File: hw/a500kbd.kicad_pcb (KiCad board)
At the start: 2 copper layers, 49.9 x 51.6 mm, 17 parts, among them J1 SERIAL, J2 AVR-ISP-6, J3 ps2ribbon, J4 ps2ribbon, SW1 SW_DPDT_x2, U1 ATmega88-20P, U2 internal keyboard, U3 ps2conn, U4 mainboard kb conn., Y1 14.7456MHz

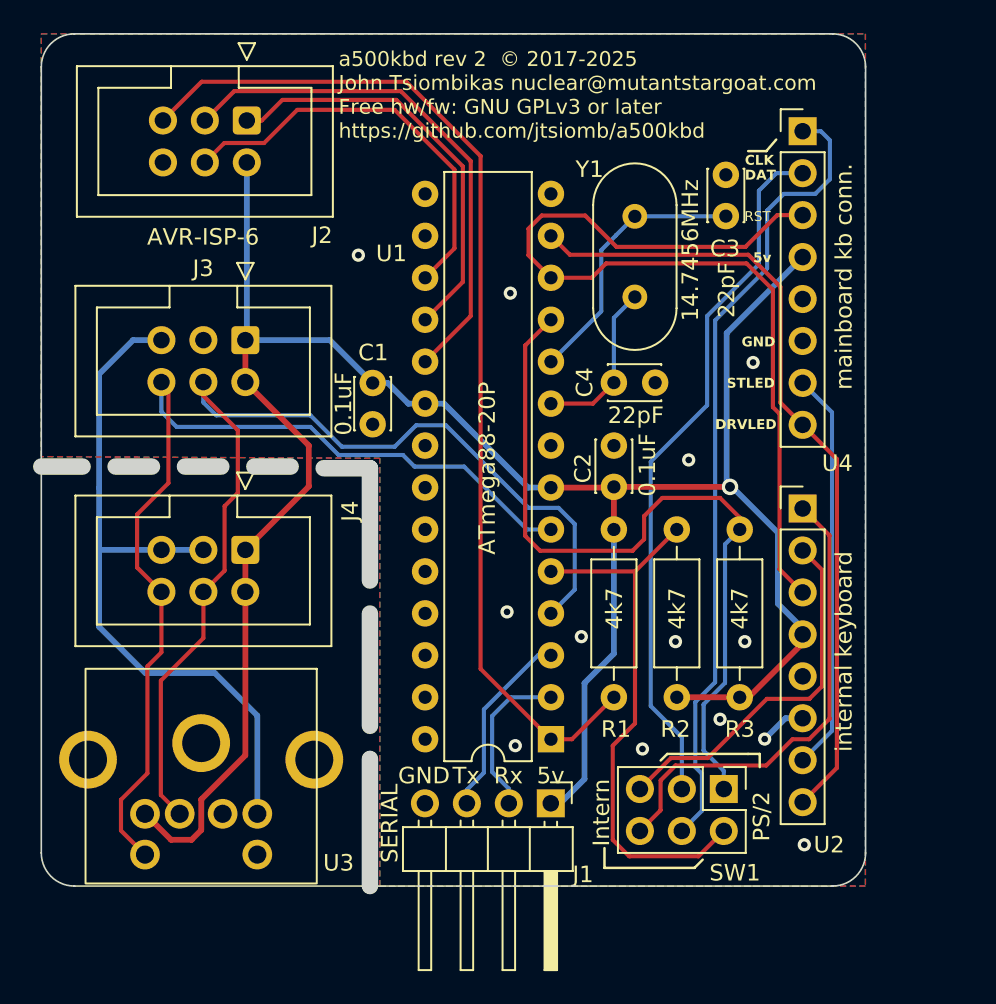
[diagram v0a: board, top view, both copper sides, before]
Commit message: fix pcb cutouts and minor re-routing of a signal
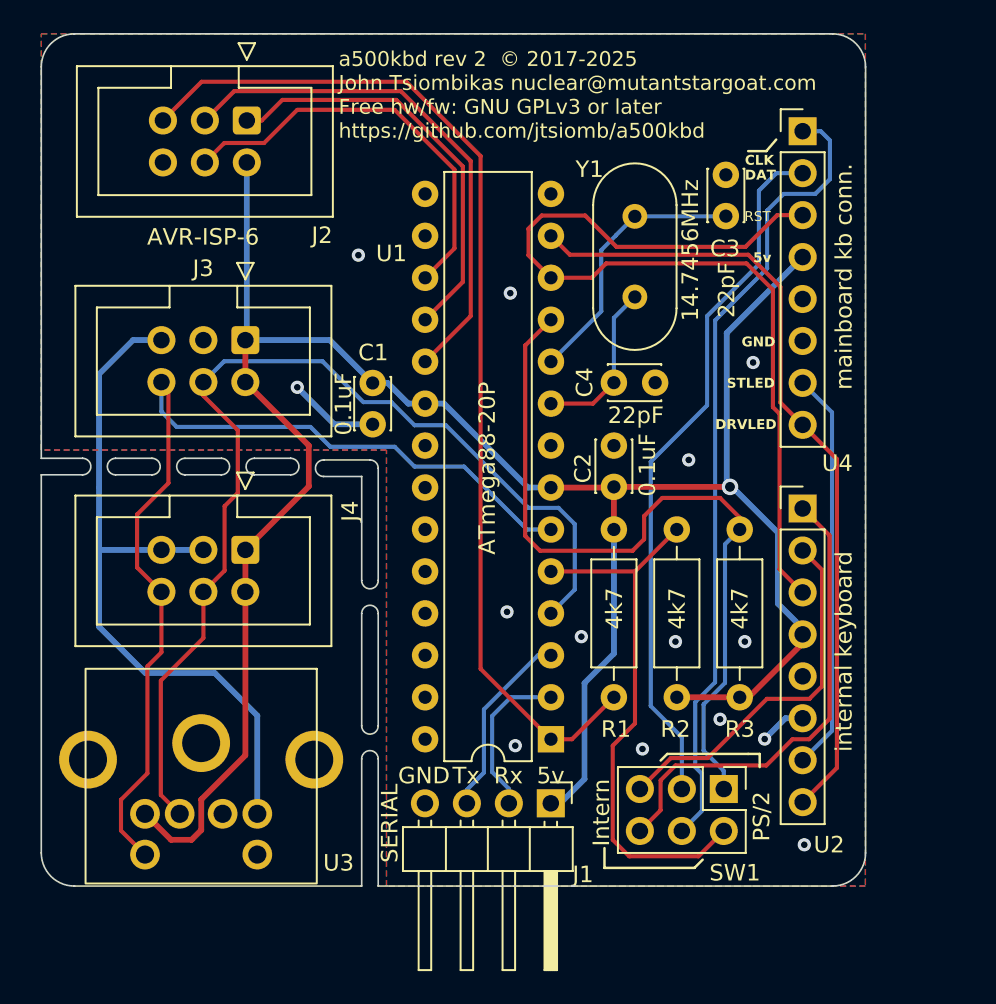
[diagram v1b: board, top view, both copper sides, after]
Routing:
- net GND: track 46.8 -> 52.3 mm, vias 13 -> 14
- net /PCLK: track 63.3 -> 62.5 mm
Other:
- outline, holes or cut-outs redrawn

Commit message: fixed (swapped) the placement of the amiga keyboard connectors
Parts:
- moved U2 23.0 mm to (152.4, 43.0)
- moved U4 22.8 mm to (152.4, 66.0)
- moved R2 10.2 mm to (144.8, 67.3), turned to -90 degrees
- moved R3 10.2 mm to (148.6, 67.3), turned to -90 degrees
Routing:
- net /ODAT: track 42.8 -> 18.9 mm
- net /OCLK: track 48.9 -> 25.2 mm
- net /INTKB_CLOCK: track 28.8 -> 49.5 mm
- net /INTKB_DATA: track 22.3 -> 42.7 mm
- net /ACLK: track 33.3 -> 20.7 mm
- net /ADATA: track 47.6 -> 37.1 mm
- net /AMIGA_RESET: track 55.6 -> 47.4 mm
- net GND: track 52.3 -> 49.5 mm, vias 14 -> 16
- net VCC: track 139.4 -> 136.9 mm, vias 1 -> 0
- net /STLED: track 24.3 -> 25.1 mm
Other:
- board text added: "CLK DAT RST VCC x GND ST DRV"
- board text added: "kb pinout"
- board text removed: "CLK"
- board text removed: "DAT"
- board text removed: "DRVLED"
- board text removed: "RST"
- board text removed: "STLED"

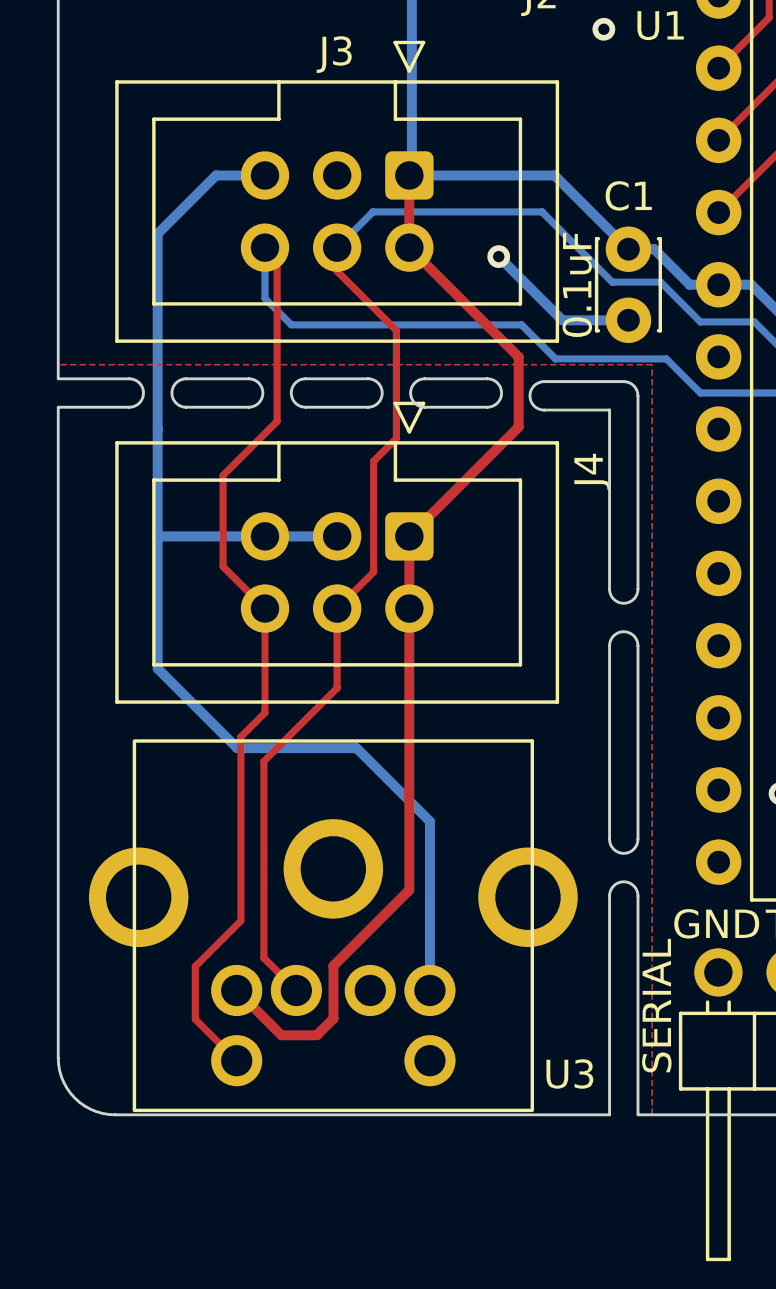
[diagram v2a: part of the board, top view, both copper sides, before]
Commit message: fixed mirrored ps2 connector in schematic
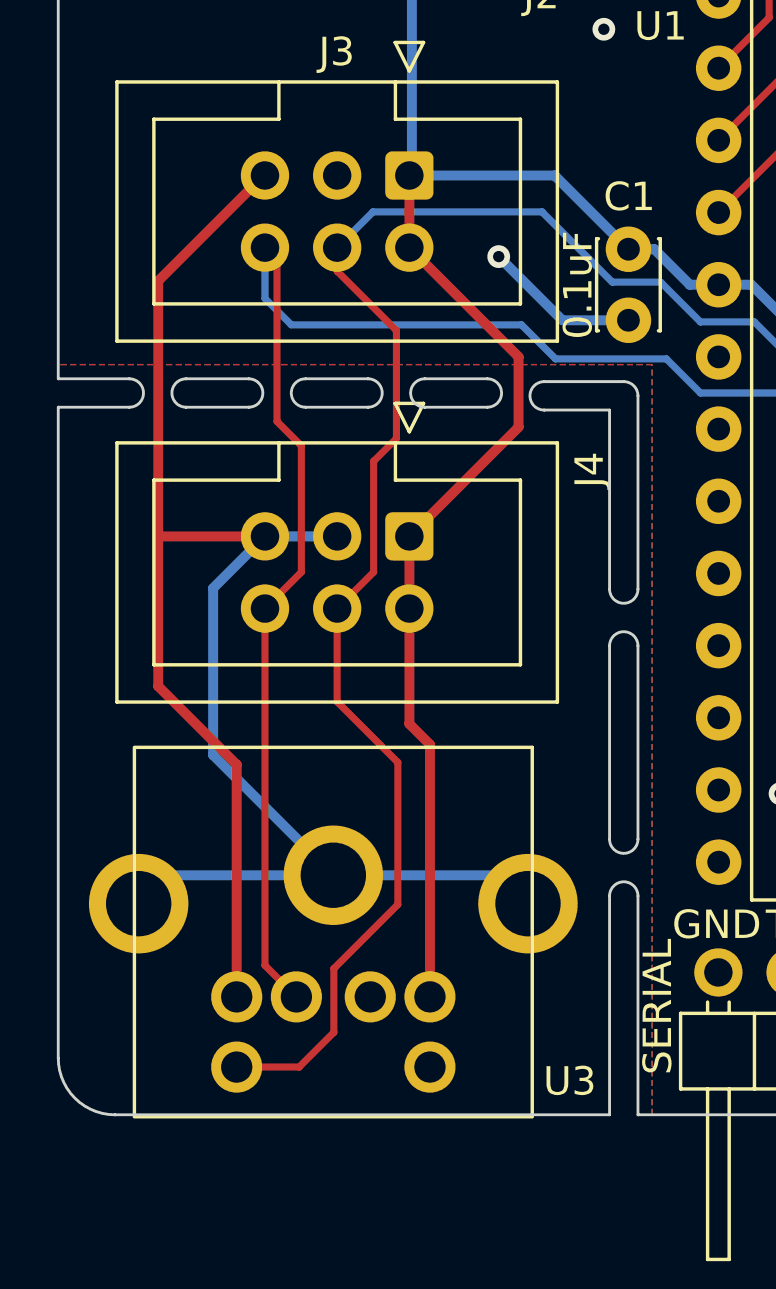
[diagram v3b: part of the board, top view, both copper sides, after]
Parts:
- moved U3 0.22 mm to (116.0, 76.0)
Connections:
- U3 pad 1: /PCLK -> /PDATA
- U3 pad 3: VCC -> GND
- U3 pad 4: GND -> VCC
- U3 pad 5: /PDATA -> /PCLK
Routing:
- net GND: track 49.5 -> 72.4 mm
- net VCC: track 136.9 -> 131.1 mm
- net /PCLK: track 62.5 -> 68.2 mm
- net /PDATA: track 60.1 -> 56.2 mm

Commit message: fixed pcb, ps/2 connector facing the wrong way
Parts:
- C1, C2: footprint Capacitor_THT:C_Disc_D3.0mm_W2.0mm_P2.50mm -> Capacitor_THT:C_Disc_D4.3mm_W1.9mm_P5.00mm
- U4: footprint Connector_PinHeader_2.54mm:PinHeader_1x08_P2.54mm_Vertical -> Connector_PinSocket_2.54mm:PinSocket_1x08_P2.54mm_Vertical
- moved U3 13.5 mm to (116.0, 89.5), turned to 0 degrees
- moved C4 3.30 mm to (144.2, 58.8), turned to -90 degrees
- moved C1 2.59 mm to (126.3, 55.9)
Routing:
- net GND: track 72.4 -> 23.5 mm, vias 16 -> 17
- net /PCLK: track 68.2 -> 56.0 mm
- net /XTAL0: track 10.1 -> 15.0 mm
- net VCC: track 131.1 -> 134.2 mm
- net /PDATA: track 56.2 -> 53.3 mm
